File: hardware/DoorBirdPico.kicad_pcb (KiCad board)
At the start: 2 copper layers, 49.3 x 68.6 mm, 22 parts, among them J0 Doorbird, J1 Reed_Door, J10 Taste A, J2 Reed_Briefkasten, J20 Taste B, J6 Conn_01x20, J8 Conn_01x20, U1 PICO_RP2040

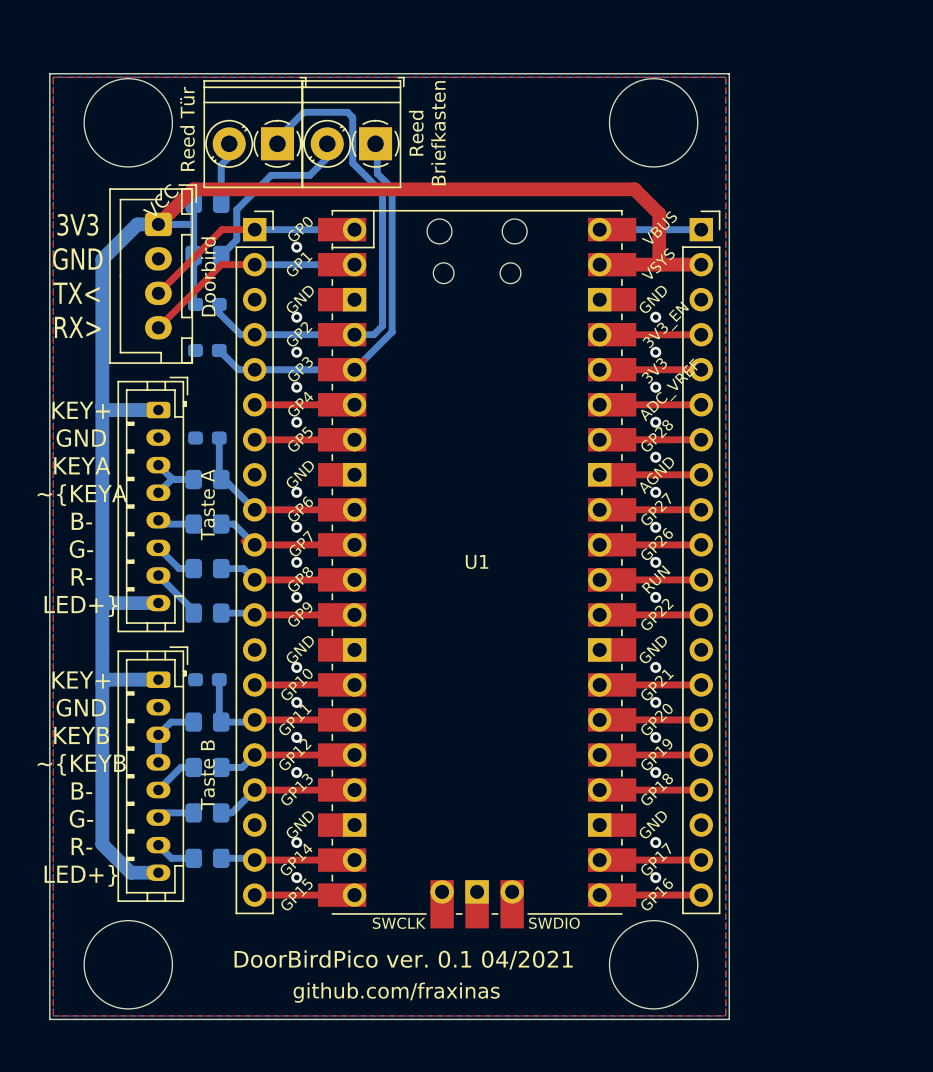
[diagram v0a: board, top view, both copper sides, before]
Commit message: PCB: Add RS485 components
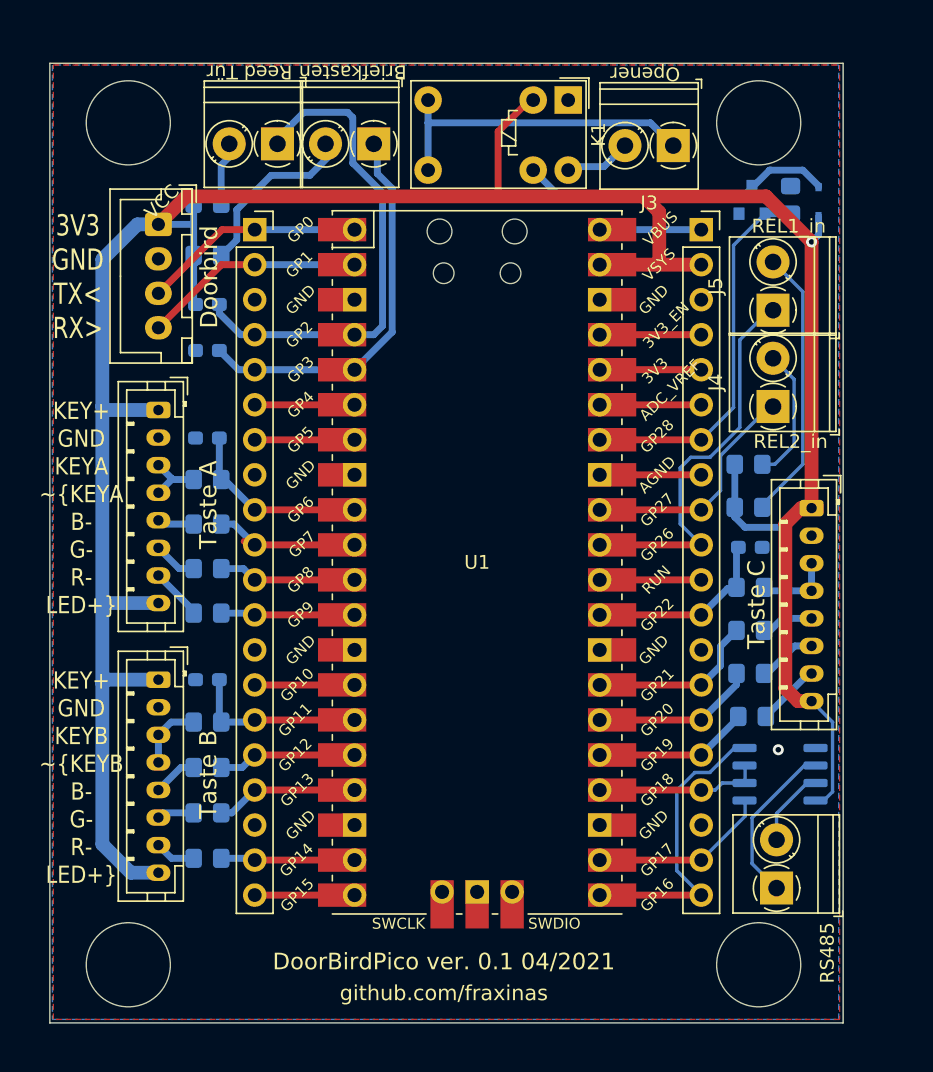
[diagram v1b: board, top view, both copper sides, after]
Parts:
- added C30: 22nF, Capacitor_SMD:C_0603_1608Metric_Pad1.08x0.95mm_HandSolder, B.Cu at (172.7, 79.3)
- added D1: 1N4148WS, Diode_SMD:D_SOD-323, B.Cu at (177.7, 54.2)
- added J3: Relay_Opener, TerminalBlock_Phoenix:TerminalBlock_Phoenix_PT-1,5-2-3.5-H_1x02_P3.50mm_Horizontal, F.Cu at (167.1, 50.2)
- added J30: Taste C, Connector_JST:JST_PH_B8B-PH-K_1x08_P2.00mm_Vertical, F.Cu at (177.2, 76.5)
- added J4: REL1_in, TerminalBlock_Phoenix:TerminalBlock_Phoenix_PT-1,5-2-3.5-H_1x02_P3.50mm_Horizontal, F.Cu at (174.4, 69.1)
- added J5: REL2_in, TerminalBlock_Phoenix:TerminalBlock_Phoenix_PT-1,5-2-3.5-H_1x02_P3.50mm_Horizontal, F.Cu at (174.4, 62.1)
- added J6: RS485, TerminalBlock_Phoenix:TerminalBlock_Phoenix_PT-1,5-2-3.5-H_1x02_P3.50mm_Horizontal, F.Cu at (174.6, 104.0)
- added K1: G5V-1, Relay_THT:Relay_SPDT_Omron_G5V-1, F.Cu at (159.5, 46.9)
- added Q1: AO3400A, Package_TO_SOT_SMD:SOT-23, B.Cu at (172.8, 54.1)
- added R3: 68k, Resistor_SMD:R_0805_2012Metric_Pad1.20x1.40mm_HandSolder, B.Cu at (175.6, 54.1)
- added R30: 12k, Resistor_SMD:R_0805_2012Metric_Pad1.20x1.40mm_HandSolder, B.Cu at (172.7, 82.2)
- added R31: 22R, Resistor_SMD:R_0805_2012Metric_Pad1.20x1.40mm_HandSolder, B.Cu at (172.7, 85.3)
- added R32: 68R, Resistor_SMD:R_0805_2012Metric_Pad1.20x1.40mm_HandSolder, B.Cu at (172.7, 88.4)
- added R33: 82R, Resistor_SMD:R_0805_2012Metric_Pad1.20x1.40mm_HandSolder, B.Cu at (172.8, 91.6)
- added R4: 68k, Resistor_SMD:R_0805_2012Metric_Pad1.20x1.40mm_HandSolder, B.Cu at (172.6, 73.3)
- added R5: 68k, Resistor_SMD:R_0805_2012Metric_Pad1.20x1.40mm_HandSolder, B.Cu at (172.6, 76.4)
- added U2: MAX3485, Package_SO:SO-8_3.9x4.9mm_P1.27mm, B.Cu at (174.9, 95.8)
- R13, R23: value 100R -> 82R
- U1: footprint DoorBirdPico:RPi_Pico_SMD_TH -> lib_includes:RPi_Pico_SMD_TH
- moved J2 0.13 mm to (145.4, 50.0)
- renumbered J8 to J98, J6 to J99
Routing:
- net +3V3: track 124.1 -> 202.9 mm, vias 0 -> 1
- net Net-(J3-Pad1): track 0.00 -> 23.5 mm
- net Net-(J5-Pad1): track 7.42 -> 30.5 mm
- net Net-(D1-Pad2): track 0.00 -> 22.7 mm
- net Net-(J98-Pad7): track 7.42 -> 27.5 mm
- net Net-(J5-Pad2): track 0.00 -> 19.9 mm
- net Net-(J98-Pad20): track 7.37 -> 22.1 mm
- net Net-(J6-Pad1): track 0.00 -> 12.3 mm
- net Net-(J4-Pad1): track 7.42 -> 17.7 mm
- net Net-(J4-Pad2): track 0.00 -> 9.79 mm
- net Net-(C30-Pad1): track 7.42 -> 13.7 mm
- net Net-(J6-Pad2): track 0.00 -> 5.91 mm
- net Net-(J98-Pad19): track 7.37 -> 13.0 mm
- net Net-(J98-Pad14): track 7.42 -> 12.4 mm
- net Net-(J30-Pad3): track 0.00 -> 5.01 mm
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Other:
- board size 49.3 x 68.6 mm -> 57.5 x 69.6 mm
- board text added: "Briefkasten"
- board text added: "Opener"
- board text removed: "Reed Briefkasten"

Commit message: Hardware: Use WAGO 250 Terminals in Schema & PCB
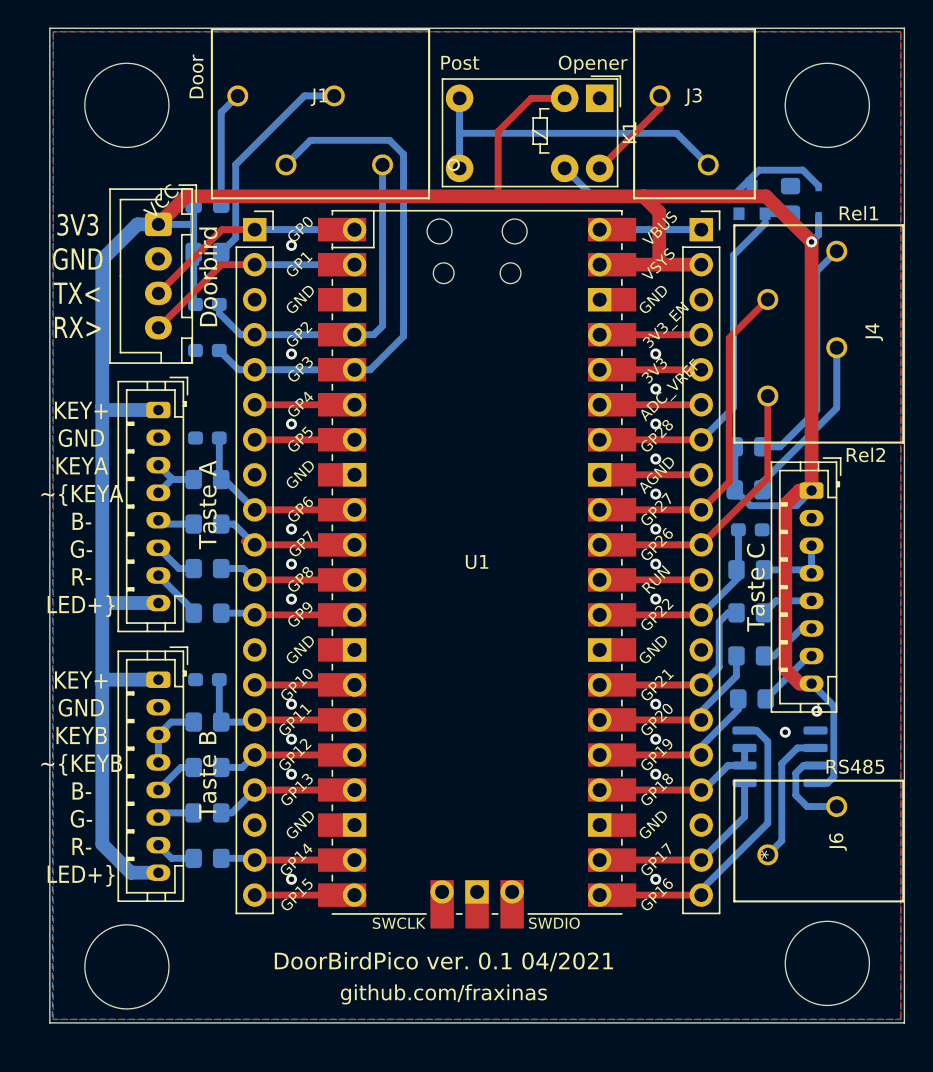
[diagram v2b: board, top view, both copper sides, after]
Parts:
- removed J2: Reed_Briefkasten, TerminalBlock_Phoenix:TerminalBlock_Phoenix_PT-1,5-2-3.5-H_1x02_P3.50mm_Horizontal
- removed J5: REL2_in, TerminalBlock_Phoenix:TerminalBlock_Phoenix_PT-1,5-2-3.5-H_1x02_P3.50mm_Horizontal
- J1: value Reed_Door -> Reed; footprint TerminalBlock_Phoenix:TerminalBlock_Phoenix_PT-1,5-2-3.5-H_1x02_P3.50mm_Horizontal -> footprints:250-204
- J3, J6: footprint TerminalBlock_Phoenix:TerminalBlock_Phoenix_PT-1,5-2-3.5-H_1x02_P3.50mm_Horizontal -> footprints:250-202
- J4: value REL1_in -> Relais_in; footprint TerminalBlock_Phoenix:TerminalBlock_Phoenix_PT-1,5-2-3.5-H_1x02_P3.50mm_Horizontal -> footprints:250-204
- moved J1 7.77 mm to (146.1, 51.6)
- moved R2 3.78 mm to (133.3, 54.4)
- moved R1 3.56 mm to (133.3, 57.9)
- moved J3 2.90 mm to (169.7, 51.6)
- moved J6 2.50 mm to (174.0, 101.6)
- moved K1 2.29 mm to (161.8, 46.7)
- moved R30 1.27 mm to (172.7, 80.9)
- moved R32 1.27 mm to (172.7, 87.2)
- moved R5 1.27 mm to (172.6, 75.1)
- moved C30 1.27 mm to (172.7, 78.0)
- moved J30 1.27 mm to (177.2, 75.2)
- moved R31 1.27 mm to (172.7, 84.1)
- moved R33 1.27 mm to (172.8, 90.3)
- moved R4 1.27 mm to (172.6, 72.0)
- moved U2 1.27 mm to (174.9, 94.5)
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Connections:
- J98 pad 10: Net-(J5-Pad1) -> Net-(J4-Pad1)
- J98 pad 9: Net-(J4-Pad1) -> Net-(J4-Pad3)
- R2 pad 2: Net-(J2-Pad2) -> Net-(J1-Pad4)
- R4 pad 1: Net-(J4-Pad2) -> Net-(J4-Pad4)
- R5 pad 1: Net-(J5-Pad2) -> Net-(J4-Pad2)
- U1 pad 31: Net-(J5-Pad1) -> Net-(J4-Pad1)
- U1 pad 32: Net-(J4-Pad1) -> Net-(J4-Pad3)
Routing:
- net Net-(J5-Pad1): track 30.5 -> 0.00 mm
- net Net-(J4-Pad3): track 0.00 -> 24.7 mm
- net Net-(J5-Pad2): track 19.9 -> 0.00 mm
- net Net-(J4-Pad4): track 0.00 -> 17.2 mm
- net Net-(J2-Pad2): track 13.1 -> 0.00 mm
- net Net-(J1-Pad2): track 4.30 -> 16.0 mm
- net Net-(C1-Pad1): track 36.2 -> 25.1 mm
- net Net-(C2-Pad1): track 28.4 -> 37.8 mm
- net Net-(J1-Pad4): track 0.00 -> 8.29 mm
- net Net-(J4-Pad2): track 9.79 -> 12.5 mm
- net Net-(J4-Pad1): track 17.7 -> 20.2 mm
- net Net-(J3-Pad2): track 4.75 -> 7.07 mm
- net Net-(J6-Pad1): track 12.3 -> 9.95 mm
- net Net-(D1-Pad2): track 22.7 -> 20.8 mm
- net Net-(J98-Pad15): track 11.4 -> 13.1 mm
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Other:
- board size 57.5 x 69.6 mm -> 62 x 72.1 mm
- board text added: "Door"
- board text added: "Post"
- board text added: "Rel1"
- board text added: "Rel2"
- board text removed: "Briefkasten"
- board text removed: "Reed Tür"

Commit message: Hardware: Add RS485 circuitry resistors
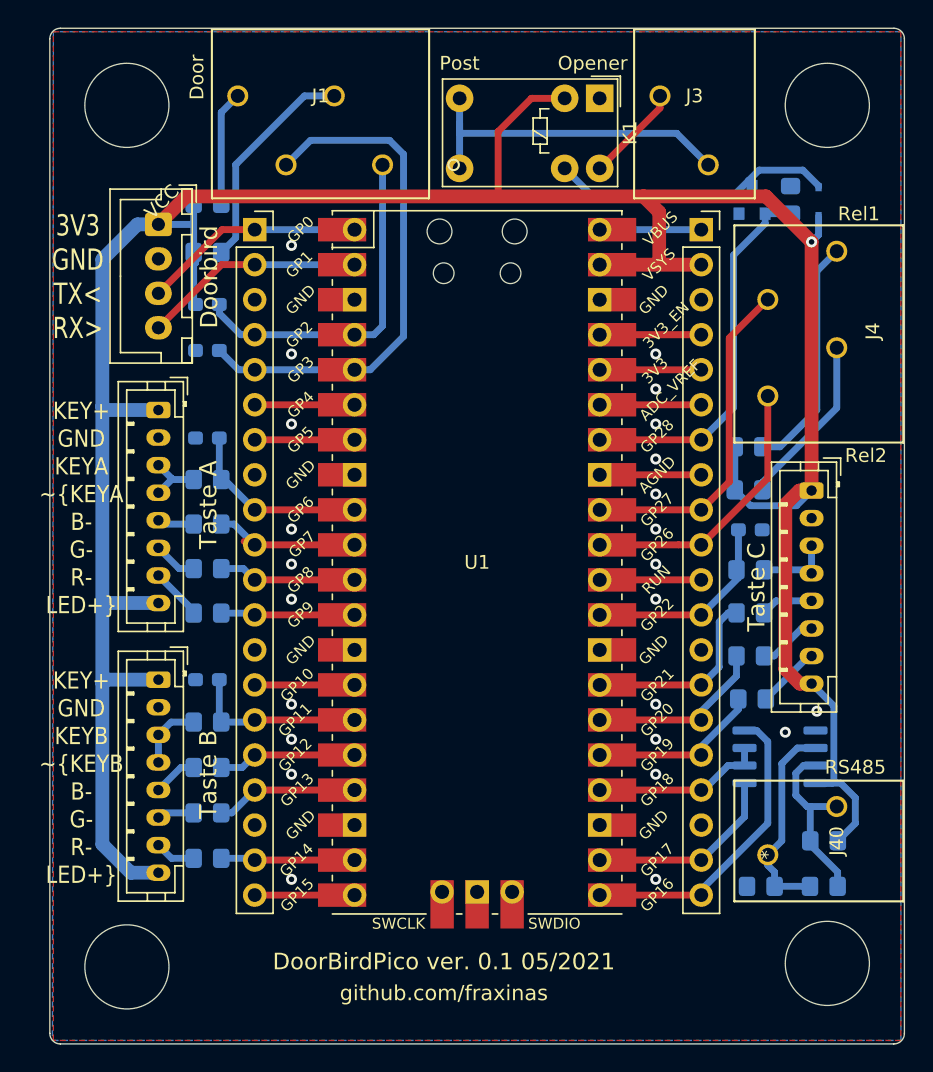
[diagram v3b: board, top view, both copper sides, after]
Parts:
- added R40: 120, Resistor_SMD:R_0805_2012Metric_Pad1.20x1.40mm_HandSolder, B.Cu at (178.1, 103.9)
- added R41: 12k, Resistor_SMD:R_0805_2012Metric_Pad1.20x1.40mm_HandSolder, B.Cu at (178.1, 100.6)
- added R42: 12k, Resistor_SMD:R_0805_2012Metric_Pad1.20x1.40mm_HandSolder, B.Cu at (173.5, 103.9)
- renumbered J6 to J40, U2 to U40
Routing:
- net +3V3: track 203.2 -> 210.4 mm
- net Net-(J40-Pad2): track 6.57 -> 13.4 mm
- net Net-(J40-Pad1): track 9.95 -> 15.3 mm
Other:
- board size 62 x 72.1 mm -> 62 x 73.7 mm
- board text added: "DoorBirdPico ver. 0.1 05/2021"
- board text added: "opt. Terminator 120R"
- board text removed: "DoorBirdPico ver. 0.1 04/2021"

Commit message: Hardware: Get ready for production
* Silkscreen label placements
* D1 handsolderable footprint
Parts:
- D1: footprint Diode_SMD:D_SOD-323 -> Diode_SMD:D_SOD-323_HandSoldering
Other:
- board text added: "Input Rel1"
- board text added: "Reed Door"
- board text added: "Reed Post"
- board text removed: "Door"
- board text removed: "Post"
- board text removed: "Rel1"

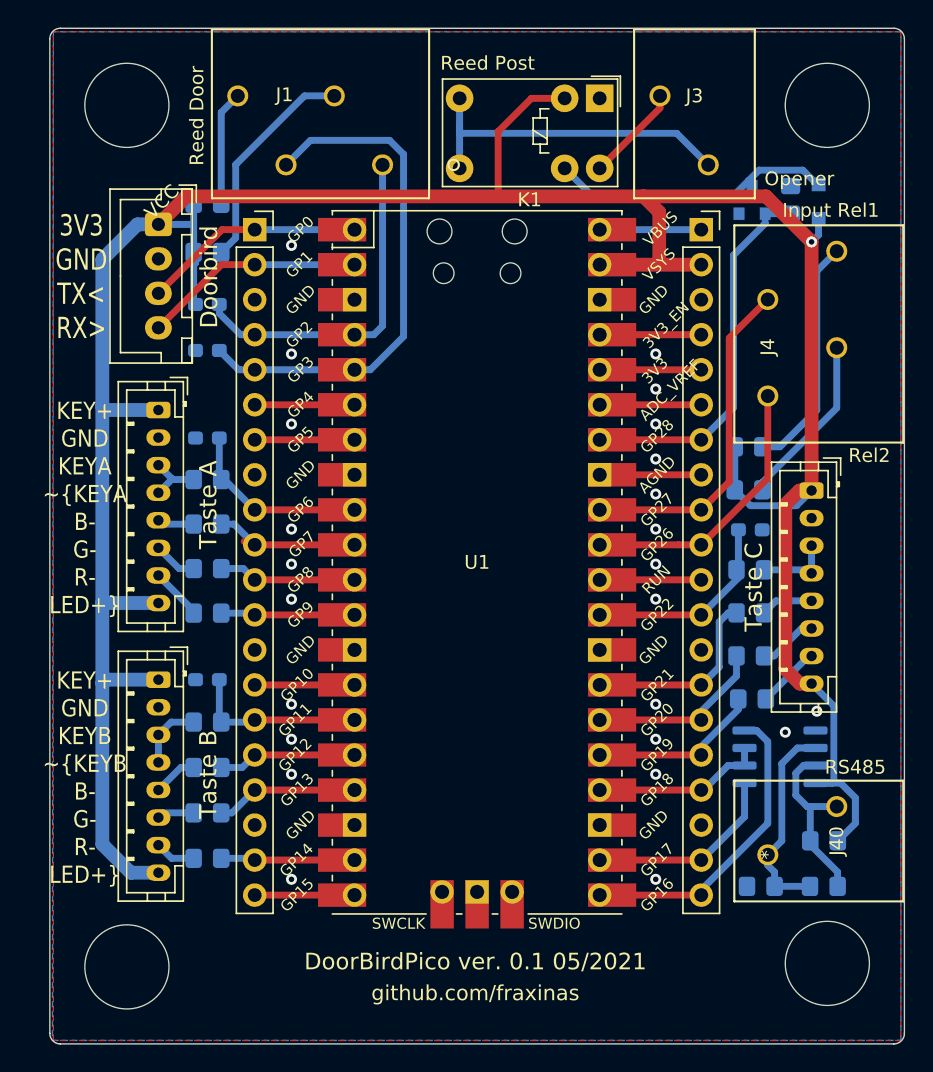
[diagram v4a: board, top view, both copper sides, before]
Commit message: PCB: Add Reset button, fix v0.2 TODOs
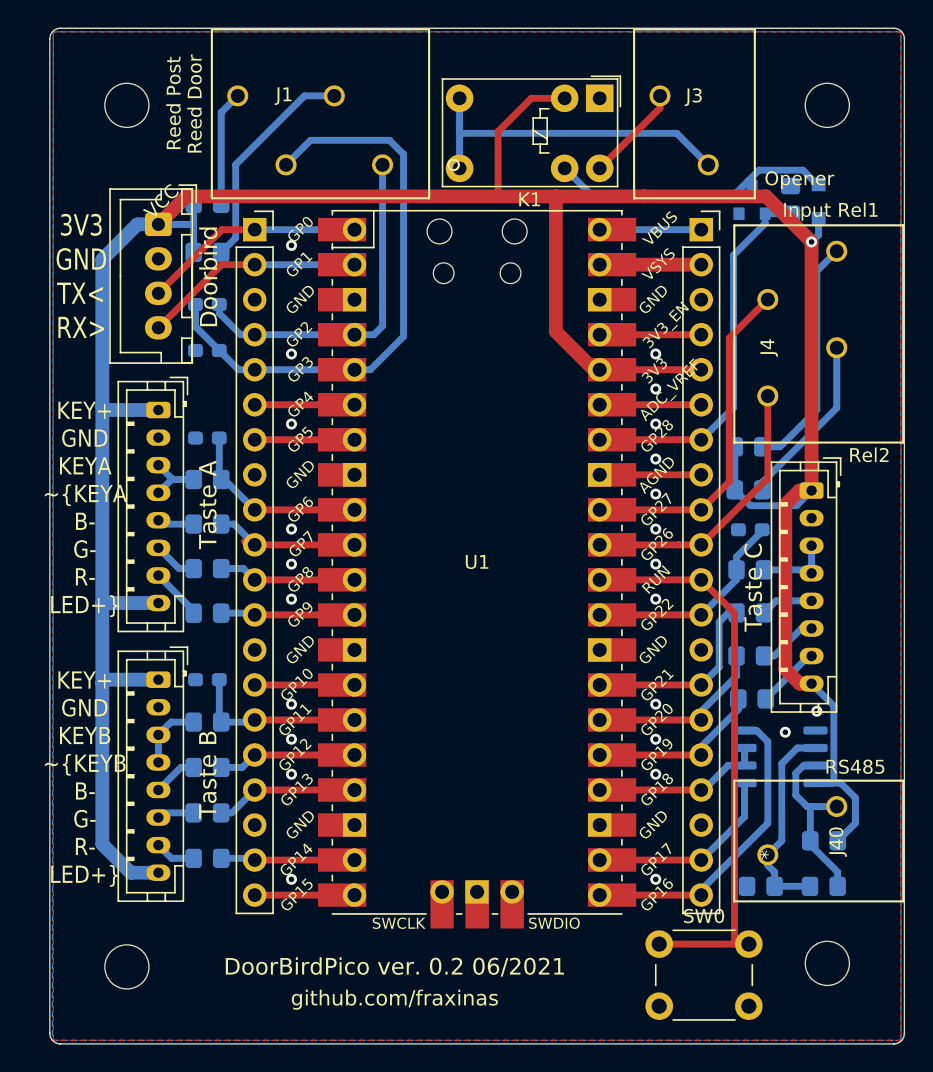
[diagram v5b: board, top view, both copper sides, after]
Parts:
- added SW0: SW_Push, Button_Switch_THT:SW_PUSH_6mm_H5mm, F.Cu at (166.1, 108.1)
- R1, R2, R4, R5: value 68k -> 100R
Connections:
- C1 pad 2: +3V3 -> Net-(C1-Pad2)
- C2 pad 1: Net-(C2-Pad1) -> Net-(C1-Pad2)
- C30 pad 1: Net-(C30-Pad1) -> GND
- C30 pad 2: GND -> Net-(C30-Pad2)
- J1 pad 3: Net-(C2-Pad1) -> Net-(C1-Pad2)
- J98 pad 12: Net-(C30-Pad1) -> Net-(C30-Pad2)
- J98 pad 2: +3V3 -> Net-(J98-Pad2)
- J98 pad 5: Net-(J98-Pad5) -> +3V3
- J99 pad 5: Net-(C2-Pad1) -> Net-(C1-Pad2)
- R30 pad 1: Net-(C30-Pad1) -> Net-(C30-Pad2)
- U1 pad 29: Net-(C30-Pad1) -> Net-(C30-Pad2)
- U1 pad 36: Net-(J98-Pad5) -> +3V3
- U1 pad 39: +3V3 -> Net-(J98-Pad2)
- U1 pad 5: Net-(C2-Pad1) -> Net-(C1-Pad2)
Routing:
- net Net-(C1-Pad2): track 0.00 -> 42.1 mm
- net Net-(C2-Pad1): track 37.8 -> 0.00 mm
- net Net-(J98-Pad11): track 7.42 -> 41.3 mm
- net Net-(C30-Pad2): track 0.00 -> 15.5 mm
- net Net-(C30-Pad1): track 14.7 -> 0.00 mm
- net Net-(J98-Pad5): track 7.42 -> 0.00 mm
- net Net-(J98-Pad2): track 0.00 -> 7.37 mm
- net +3V3: track 210.4 -> 215.4 mm
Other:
- outline, holes or cut-outs redrawn
- board text added: "DoorBirdPico ver. 0.2 06/2021"
- board text removed: "DoorBirdPico ver. 0.1 05/2021"
